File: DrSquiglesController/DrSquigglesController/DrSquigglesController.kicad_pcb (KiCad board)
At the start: 2 copper layers, 40.6 x 59.7 mm, 7 parts, among them J1 Conn_01x04, J2 Conn_01x02, J3 Conn_02x08_Odd_Even, J4 Screw_Terminal_01x02, U1 teensy_3_2, U2 D24V22F5, U3 ULN2803A

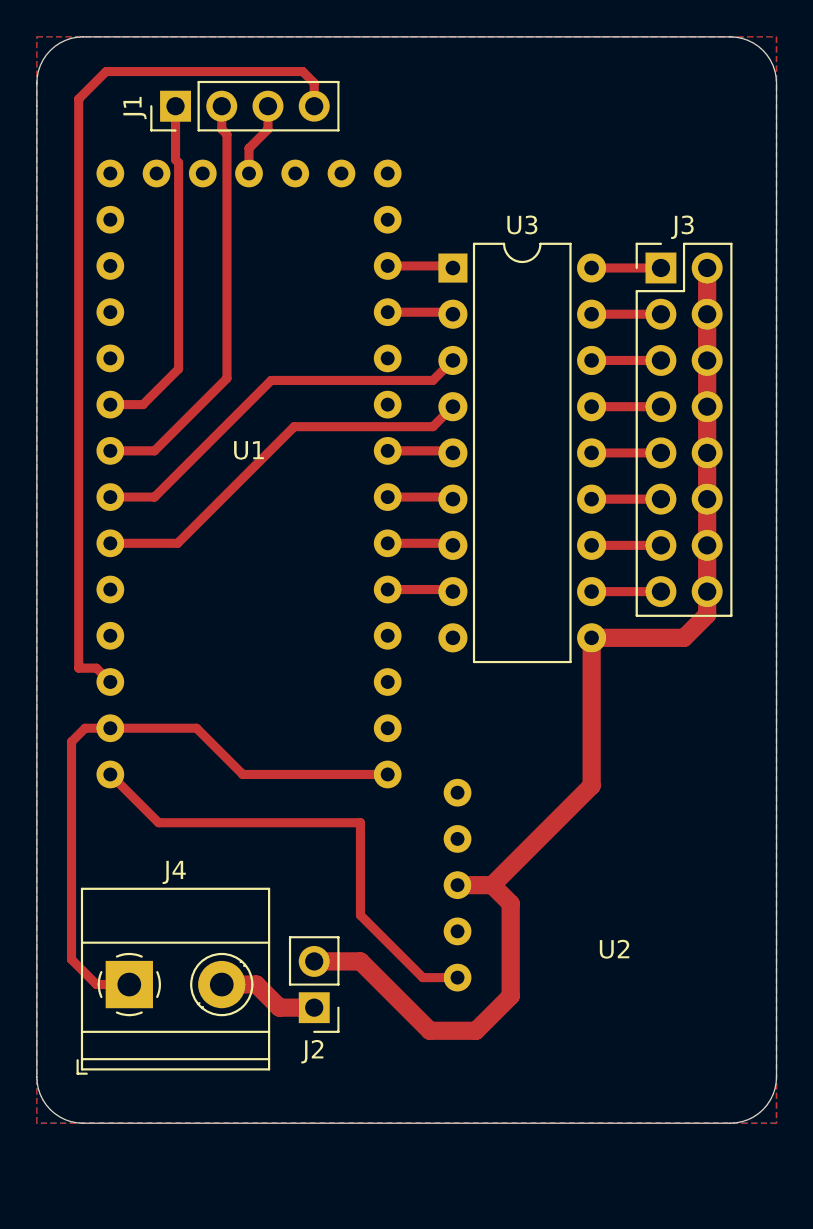
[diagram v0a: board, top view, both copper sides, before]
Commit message: replaced screw terminal to make space for conecting teensy3.2 USB
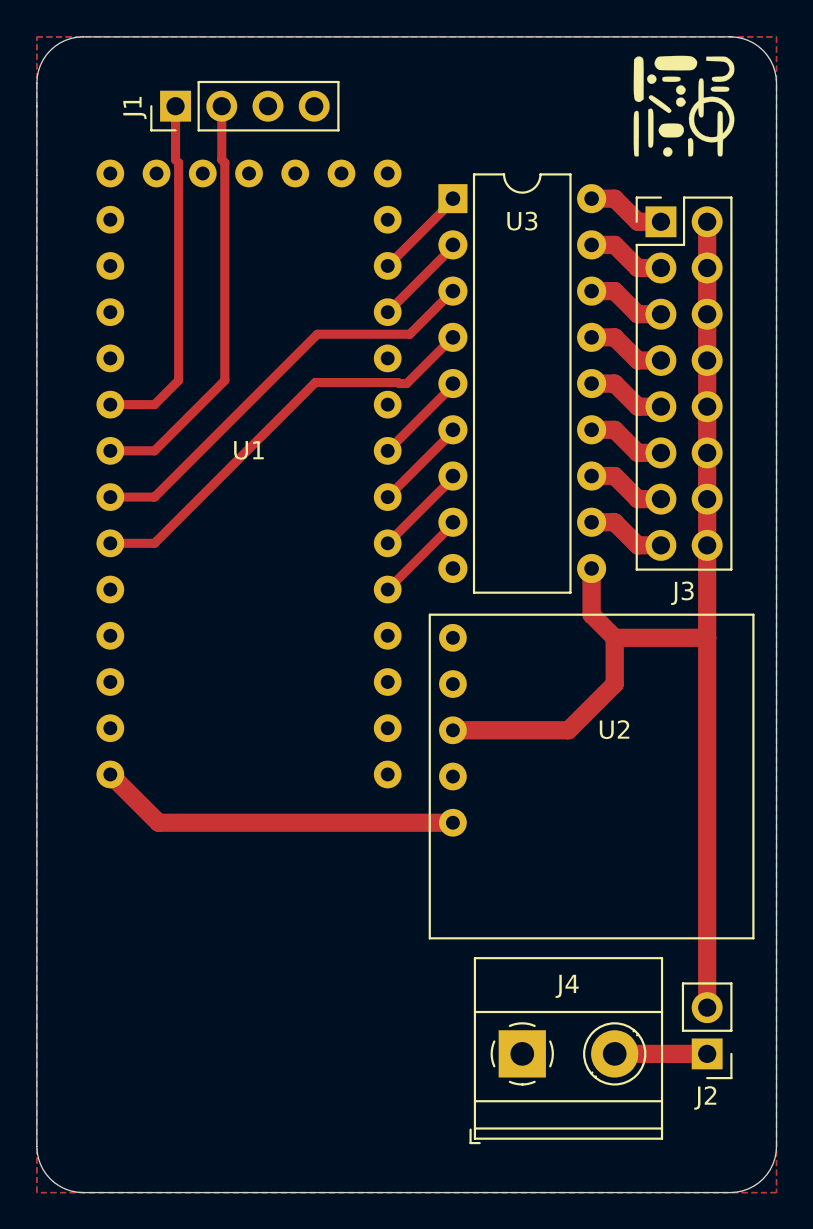
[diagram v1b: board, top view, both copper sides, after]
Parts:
- added G***: LOGO, Footprint:RITMO_logo, F.Cu at (139.7, 59.7)
- moved J4 21.9 mm to (130.8, 111.8)
- moved J2 21.7 mm to (141.0, 111.8)
- moved U2 15.0 mm to (127.0, 88.9)
- moved U3 3.81 mm to (127.0, 64.8)
- moved J3 2.54 mm to (138.4, 66.0)
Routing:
- net 3V3: track 48.4 -> 0.00 mm
- net GND: track 38.6 -> 0.00 mm
- net Net-(U1-Pad33): track 26.7 -> 19.9 mm
- net V12: track 63.4 -> 65.1 mm
- net mi4: track 21.9 -> 23.6 mm
- net mi3: track 21.9 -> 23.5 mm
- net mi8: track 3.63 -> 5.18 mm
- net mi1: track 3.63 -> 5.18 mm
- net mi6: track 3.63 -> 5.18 mm
- net mi7: track 3.63 -> 5.18 mm
- net mi5: track 3.63 -> 5.18 mm
- net mi2: track 3.63 -> 5.18 mm
- net Net-(J3-Pad5): track 3.81 -> 4.34 mm
- net Net-(J3-Pad1): track 3.81 -> 4.34 mm
- net Net-(J3-Pad9): track 3.81 -> 4.34 mm
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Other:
- board size 40.6 x 59.7 mm -> 40.6 x 63.5 mm
- board text added: "Dr. Squiggles Controller Board v1.0"

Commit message: added jumper for raspi power
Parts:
- removed G***: LOGO, Footprint:RITMO_logo
- added J5: Conn_01x02, Connector_PinHeader_2.54mm:PinHeader_1x02_P2.54mm_Vertical, F.Cu at (124.5, 111.8)
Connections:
- net Net-(U1-Pad33) renamed 5V
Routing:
- net 5V: track 19.9 -> 31.1 mm

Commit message: added RITMO logo again
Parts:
- added G***: LOGO, Footprint:RITMO_logo, F.Cu at (139.7, 59.7)
